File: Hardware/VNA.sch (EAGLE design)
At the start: 502 parts, among them IC1 MIC2253, IC10 MAX2871, IC11 RFSW6042, IC12 RFSW6042, IC13 QPC6324, IC14 RFSA3714, IC15 TRF37A73, IC16 QPC6324, IC17 QPC6324, IC18 QPC6324, IC19 AP2114H, IC2 LM3370SD-4221, IC20 NCP702-3.3, IC21 MAX2871, IC22 LT5560, IC23 THS4521IDGKR, IC24 ADL5801, IC25 NCP702-1.8, IC26 MCP33131D-10-E/MS, IC27 LT5560, IC28 THS4521IDGKR, IC29 ADL5801, IC3 LDL212PU50R, IC30 NCP702-1.8, IC31 MCP33131D-10-E/MS, IC32 THS4521IDGKR, IC33 ADL5801, IC34 NCP702-1.8, IC35 MCP33131D-10-E/MS, IC36 LT5560, IC37 STM32G431CB, IC4 LDL212PU50R, IC5 LDL212PU50R, IC6 LDL212PU50R, IC7 SI5351C, IC8 AP2114H, IC9 NCP702-3.3, J1 DNP, J2 AMPHENOL_132289, J3 AMPHENOL_132289, J4 TYPE-C16P(073), Q1 FA-128 26MHz, T1 B012-617DB-1-63-B331, T2 B012-617DB-1-63-B331, T3 B012-617DB-1-63-B331, U1 W25Q16BVSN, U2 6SLX9TQG144, X1 SMA_CONNECTOR, X2 SMA_CONNECTOR, X3 DNP

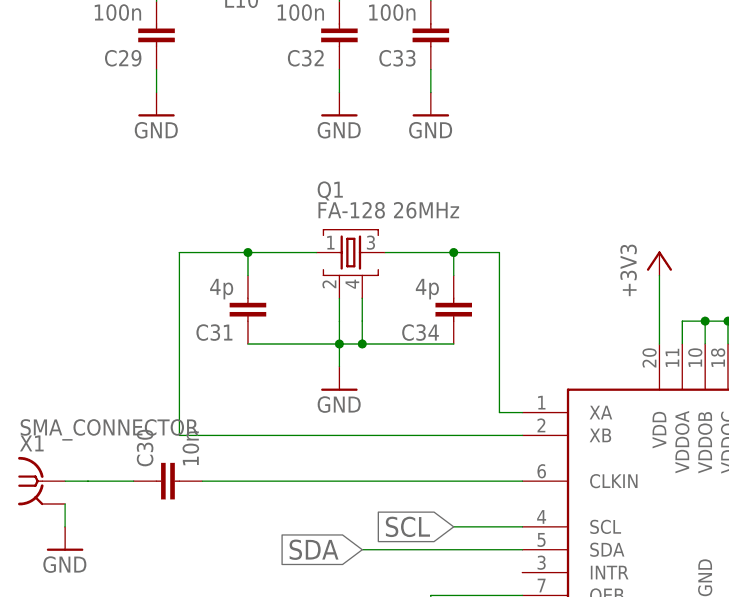
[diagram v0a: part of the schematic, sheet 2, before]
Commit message: TCXO instead of crystal
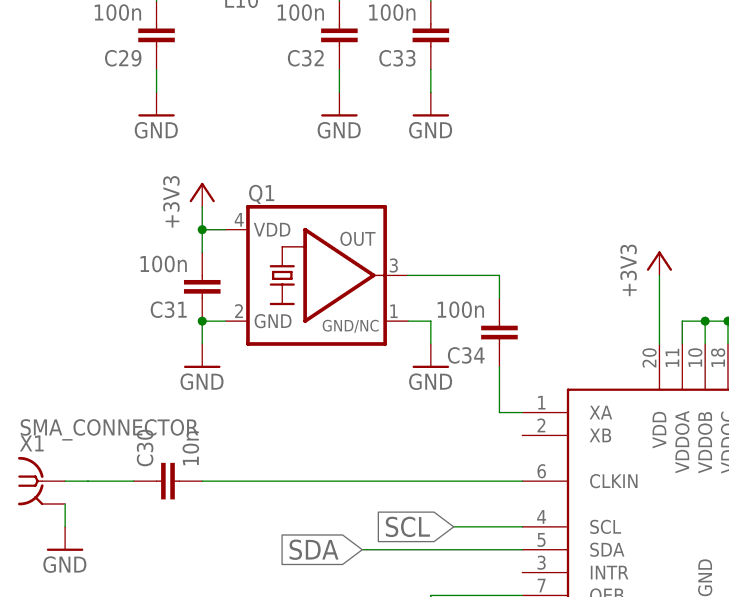
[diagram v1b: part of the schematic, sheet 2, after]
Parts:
- C31, C34: value 4p -> 100n
- Q1: value FA-128 26MHz -> DSB221SDN/26MHz; device VNA:FA-128 -> crystal-geyer_V1_0:KXO-TCXO-CMOS-86
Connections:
- net +3V3: now also C31.2, Q1.VDD
- net GND: now also Q1.GND, Q1.GND/NC; no longer C34.1, Q1.2, Q1.4
- net N$113: now also Q1.OUT; no longer IC7.XA, Q1.3
- net N$114: now also C34.1, IC7.XA; no longer C31.2, IC7.XB, Q1.1
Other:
- moved on the sheet: C31, C34
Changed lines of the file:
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@@
 <part name="R6" library="VNA" library_urn="urn:adsk.eagle:library:22367181" deviceset="R-EU_" device="R0402" package3d_urn="urn:adsk.eagle:package:22367274/2" value="10k"/>
 <part name="GND47" library="VNA" library_urn="urn:adsk.eagle:library:22367181" deviceset="GND" device=""/>
-<part name="Q1" library="VNA" library_urn="urn:adsk.eagle:library:22367181" deviceset="FA-" device="128" package3d_urn="urn:adsk.eagle:package:22367298/2" value="FA-128 26MHz"/>
-<part name="C31" library="VNA" library_urn="urn:adsk.eagle:library:22367181" deviceset="C-EU*?:2" device="C0402" package3d_urn="urn:adsk.eagle:package:22367275/2" value="4p"/>
-<part name="C34" library="VNA" library_urn="urn:adsk.eagle:library:22367181" deviceset="C-EU*?:2" device="C0402" package3d_urn="urn:adsk.eagle:package:22367275/2" value="4p"/>
+<part name="C31" library="VNA" library_urn="urn:adsk.eagle:library:22367181" deviceset="C-EU*?:2" device="C0402" package3d_urn="urn:adsk.eagle:package:22367275/2" value="100n"/>
+<part name="C34" library="VNA" library_urn="urn:adsk.eagle:library:22367181" deviceset="C-EU*?:2" device="C0402" package3d_urn="urn:adsk.eagle:package:22367275/2" value="100n"/>
 <part name="GND45" library="VNA" library_urn="urn:adsk.eagle:library:22367181" deviceset="GND" device=""/>
 <part name="L10" library="VNA" library_urn="urn:adsk.eagle:library:22367181" deviceset="INDUCTOR" device="0402" package3d_urn="urn:adsk.eagle:package:22367307/2" value="Ferrite"/>
@@
 <part name="C6" library="VNA" library_urn="urn:adsk.eagle:library:22367181" deviceset="C-EU*?:2" device="C0402" package3d_urn="urn:adsk.eagle:package:22367275/2" value="100n"/>
 <part name="GND13" library="VNA" library_urn="urn:adsk.eagle:library:22367181" deviceset="GND" device=""/>
+<part name="Q1" library="crystal-geyer_V1_0" library_urn="urn:adsk.eagle:library:203" deviceset="KXO-TCXO-CMOS" device="-86" package3d_urn="urn:adsk.eagle:package:11955/1" value="DSB221SDN/26MHz"/>
+<part name="GND262" library="VNA" library_urn="urn:adsk.eagle:library:22367181" deviceset="GND" device=""/>
+<part name="+3V1" library="VNA" library_urn="urn:adsk.eagle:library:22367181" deviceset="+3V3" device=""/>
 </parts>
 <sheets>
@@
 <attribute name="VALUE" x="91.44" y="106.68" size="1.778" layer="96"/>
 </instance>
-<instance part="Q1" gate="G$1" x="83.82" y="165.1" smashed="yes">
-<attribute name="NAME" x="81.28" y="171.196" size="1.778" layer="95"/>
-<attribute name="VALUE" x="81.28" y="168.91" size="1.778" layer="96"/>
-</instance>
-<instance part="C31" gate="G$1" x="73.66" y="157.48" smashed="yes" rot="R180">
-<attribute name="NAME" x="72.136" y="157.099" size="1.778" layer="95" rot="R180"/>
-<attribute name="VALUE" x="72.136" y="162.179" size="1.778" layer="96" rot="R180"/>
-</instance>
-<instance part="C34" gate="G$1" x="96.52" y="157.48" smashed="yes" rot="R180">
-<attribute name="NAME" x="94.996" y="157.099" size="1.778" layer="95" rot="R180"/>
-<attribute name="VALUE" x="94.996" y="162.179" size="1.778" layer="96" rot="R180"/>
-</instance>
-<instance part="GND45" gate="1" x="83.82" y="149.86" smashed="yes">
-<attribute name="VALUE" x="81.28" y="147.32" size="1.778" layer="96"/>
+<instance part="C31" gate="G$1" x="68.58" y="160.02" smashed="yes" rot="R180">
+<attribute name="NAME" x="67.056" y="159.639" size="1.778" layer="95" rot="R180"/>
+<attribute name="VALUE" x="67.056" y="164.719" size="1.778" layer="96" rot="R180"/>
+</instance>
+<instance part="C34" gate="G$1" x="101.6" y="154.94" smashed="yes" rot="R180">
+<attribute name="NAME" x="100.076" y="154.559" size="1.778" layer="95" rot="R180"/>
+<attribute name="VALUE" x="100.076" y="159.639" size="1.778" layer="96" rot="R180"/>
+</instance>
+<instance part="GND45" gate="1" x="68.58" y="152.4" smashed="yes">
+<attribute name="VALUE" x="66.04" y="149.86" size="1.778" layer="96"/>
 </instance>
 <instance part="L10" gate="G$1" x="71.12" y="195.58" smashed="yes" rot="R90">
@@
 <instance part="GND61" gate="1" x="259.08" y="88.9" smashed="yes">
 <attribute name="VALUE" x="256.54" y="86.36" size="1.778" layer="96"/>
+</instance>
+<instance part="Q1" gate="G$1" x="81.28" y="162.56" smashed="yes">
+<attribute name="NAME" x="73.66" y="170.815" size="1.778" layer="95"/>
+</instance>
+<instance part="GND262" gate="1" x="93.98" y="152.4" smashed="yes">
+<attribute name="VALUE" x="91.44" y="149.86" size="1.778" layer="96"/>
+</instance>
+<instance part="+3V1" gate="G$1" x="68.58" y="172.72" smashed="yes">
+<attribute name="VALUE" x="66.04" y="167.64" size="1.778" layer="96" rot="R90"/>
 </instance>
 </instances>
@@
 </segment>
 <segment>
-<pinref part="Q1" gate="G$1" pin="2"/>
-<wire x1="83.82" y1="160.02" x2="83.82" y2="157.48" width="0.1524" layer="91"/>
-<pinref part="GND45" gate="1" pin="GND"/>
-<wire x1="83.82" y1="152.4" x2="83.82" y2="154.94" width="0.1524" layer="91"/>
-<pinref part="C31" gate="G$1" pin="1"/>
-<wire x1="83.82" y1="154.94" x2="83.82" y2="157.48" width="0.1524" layer="91"/>
-<wire x1="73.66" y1="154.94" x2="83.82" y2="154.94" width="0.1524" layer="91"/>
-<junction x="83.82" y="154.94"/>
-<pinref part="C34" gate="G$1" pin="1"/>
-<wire x1="83.82" y1="154.94" x2="86.36" y2="154.94" width="0.1524" layer="91"/>
-<pinref part="Q1" gate="G$1" pin="4"/>
-<wire x1="86.36" y1="154.94" x2="96.52" y2="154.94" width="0.1524" layer="91"/>
-<wire x1="86.36" y1="157.48" x2="86.36" y2="160.02" width="0.1524" layer="91"/>
-<wire x1="86.36" y1="157.48" x2="86.36" y2="154.94" width="0.1524" layer="91"/>
-<junction x="86.36" y="154.94"/>
-</segment>
-<segment>
 <pinref part="GND43" gate="1" pin="GND"/>
 <pinref part="C29" gate="G$1" pin="1"/>
@@
 <pinref part="C47" gate="G$1" pin="2"/>
 <pinref part="GND61" gate="1" pin="GND"/>
+</segment>
+<segment>
+<pinref part="Q1" gate="G$1" pin="GND/NC"/>
+<pinref part="GND262" gate="1" pin="GND"/>
+<wire x1="91.44" y1="157.48" x2="93.98" y2="157.48" width="0.1524" layer="91"/>
+<wire x1="93.98" y1="157.48" x2="93.98" y2="154.94" width="0.1524" layer="91"/>
+</segment>
+<segment>
+<pinref part="GND45" gate="1" pin="GND"/>
+<pinref part="C31" gate="G$1" pin="1"/>
+<wire x1="68.58" y1="154.94" x2="68.58" y2="157.48" width="0.1524" layer="91"/>
+<pinref part="Q1" gate="G$1" pin="GND"/>
+<wire x1="71.12" y1="157.48" x2="68.58" y2="157.48" width="0.1524" layer="91"/>
+<junction x="68.58" y="157.48"/>
 </segment>
 </net>
@@
 <wire x1="93.98" y1="127" x2="104.14" y2="127" width="0.1524" layer="91"/>
 <pinref part="R6" gate="G$1" pin="2"/>
-</segment>
-</net>
-<net name="N$113" class="0">
-<segment>
-<pinref part="C34" gate="G$1" pin="2"/>
-<pinref part="Q1" gate="G$1" pin="3"/>
-<wire x1="96.52" y1="162.56" x2="96.52" y2="165.1" width="0.1524" layer="91"/>
-<wire x1="96.52" y1="165.1" x2="88.9" y2="165.1" width="0.1524" layer="91"/>
-<wire x1="96.52" y1="165.1" x2="101.6" y2="165.1" width="0.1524" layer="91"/>
-<wire x1="101.6" y1="165.1" x2="101.6" y2="147.32" width="0.1524" layer="91"/>
-<junction x="96.52" y="165.1"/>
-<pinref part="IC7" gate="G$1" pin="XA"/>
-<wire x1="101.6" y1="147.32" x2="104.14" y2="147.32" width="0.1524" layer="91"/>
-</segment>
-</net>
-<net name="N$114" class="0">
-<segment>
-<pinref part="Q1" gate="G$1" pin="1"/>
-<pinref part="C31" gate="G$1" pin="2"/>
-<wire x1="81.28" y1="165.1" x2="73.66" y2="165.1" width="0.1524" layer="91"/>
-<wire x1="73.66" y1="165.1" x2="73.66" y2="162.56" width="0.1524" layer="91"/>
-<pinref part="IC7" gate="G$1" pin="XB"/>
-<wire x1="104.14" y1="144.78" x2="66.04" y2="144.78" width="0.1524" layer="91"/>
-<wire x1="66.04" y1="144.78" x2="66.04" y2="165.1" width="0.1524" layer="91"/>
-<wire x1="66.04" y1="165.1" x2="73.66" y2="165.1" width="0.1524" layer="91"/>
-<junction x="73.66" y="165.1"/>
 </segment>
 </net>
@@
 <wire x1="119.38" y1="162.56" x2="119.38" y2="154.94" width="0.1524" layer="91"/>
 </segment>
+<segment>
+<pinref part="Q1" gate="G$1" pin="VDD"/>
+<wire x1="71.12" y1="167.64" x2="68.58" y2="167.64" width="0.1524" layer="91"/>
+<pinref part="C31" gate="G$1" pin="2"/>
+<wire x1="68.58" y1="167.64" x2="68.58" y2="165.1" width="0.1524" layer="91"/>
+<pinref part="+3V1" gate="G$1" pin="+3V3"/>
+<wire x1="68.58" y1="170.18" x2="68.58" y2="167.64" width="0.1524" layer="91"/>
+<junction x="68.58" y="167.64"/>
+</segment>
 </net>
 <net name="SCL" class="0">
@@
 </segment>
 </net>
+<net name="N$113" class="0">
+<segment>
+<pinref part="Q1" gate="G$1" pin="OUT"/>
+<pinref part="C34" gate="G$1" pin="2"/>
+<wire x1="91.44" y1="162.56" x2="101.6" y2="162.56" width="0.1524" layer="91"/>
+<wire x1="101.6" y1="162.56" x2="101.6" y2="160.02" width="0.1524" layer="91"/>
+</segment>
+</net>
+<net name="N$114" class="0">
+<segment>
+<pinref part="IC7" gate="G$1" pin="XA"/>
+<pinref part="C34" gate="G$1" pin="1"/>
+<wire x1="104.14" y1="147.32" x2="101.6" y2="147.32" width="0.1524" layer="91"/>
+<wire x1="101.6" y1="147.32" x2="101.6" y2="152.4" width="0.1524" layer="91"/>
+</segment>
+</net>

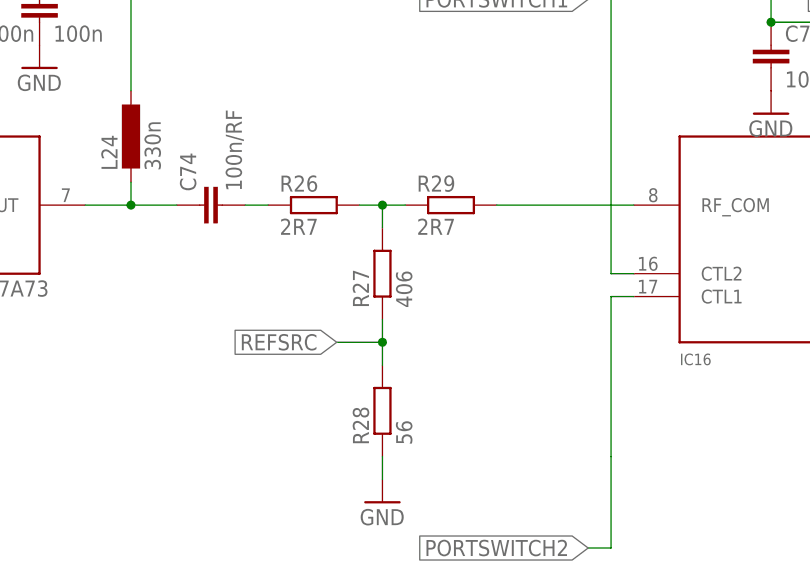
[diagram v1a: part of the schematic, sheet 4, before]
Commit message: R27 value fixed
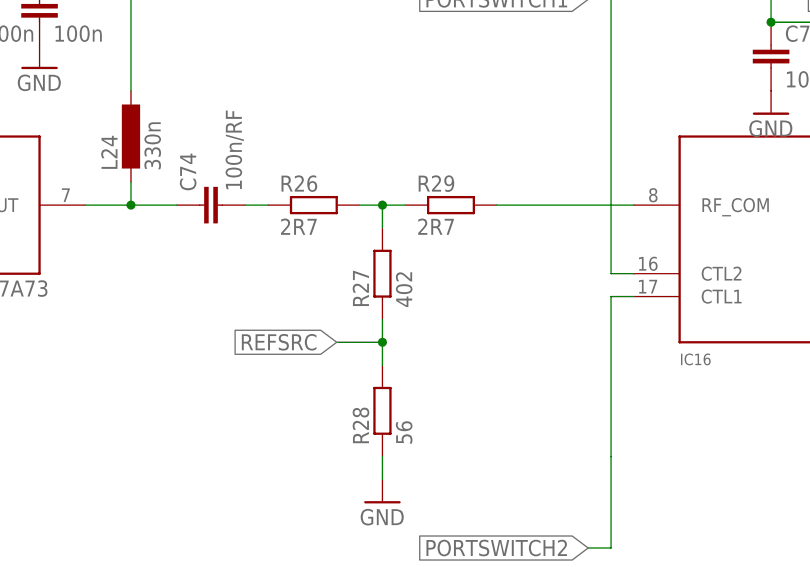
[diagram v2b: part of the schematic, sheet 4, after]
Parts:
- R27: value 406 -> 402
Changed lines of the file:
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@@
 <part name="R26" library="VNA" library_urn="urn:adsk.eagle:library:22367181" deviceset="R-EU_" device="R0402" package3d_urn="urn:adsk.eagle:package:22367274/2" value="2R7"/>
 <part name="R29" library="VNA" library_urn="urn:adsk.eagle:library:22367181" deviceset="R-EU_" device="R0402" package3d_urn="urn:adsk.eagle:package:22367274/2" value="2R7"/>
-<part name="R27" library="VNA" library_urn="urn:adsk.eagle:library:22367181" deviceset="R-EU_" device="R0402" package3d_urn="urn:adsk.eagle:package:22367274/2" value="406"/>
+<part name="R27" library="VNA" library_urn="urn:adsk.eagle:library:22367181" deviceset="R-EU_" device="R0402" package3d_urn="urn:adsk.eagle:package:22367274/2" value="402"/>
 <part name="R28" library="VNA" library_urn="urn:adsk.eagle:library:22367181" deviceset="R-EU_" device="R0402" package3d_urn="urn:adsk.eagle:package:22367274/2" value="56"/>
 <part name="GND103" library="VNA" library_urn="urn:adsk.eagle:library:22367181" deviceset="GND" device=""/>

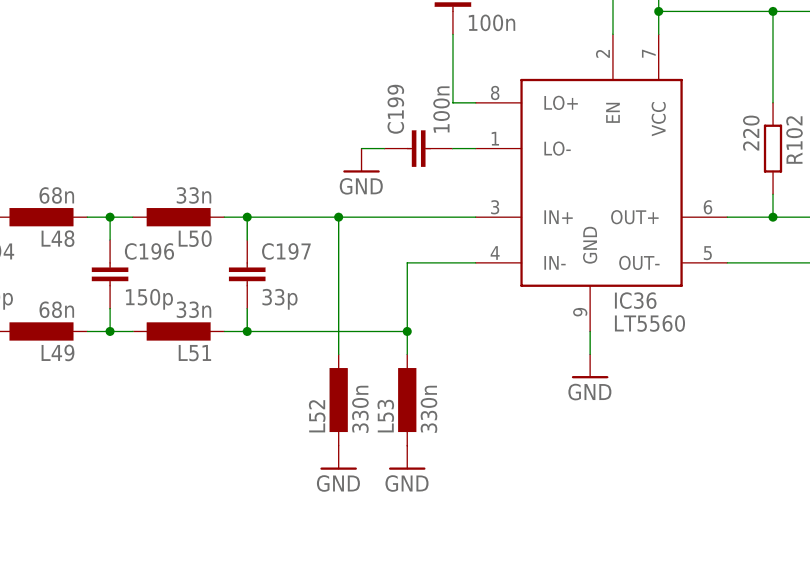
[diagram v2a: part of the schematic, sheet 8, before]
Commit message: Footprint adjustments for THS4521/0402 inductors, fixed mixup of CCLK/DIN
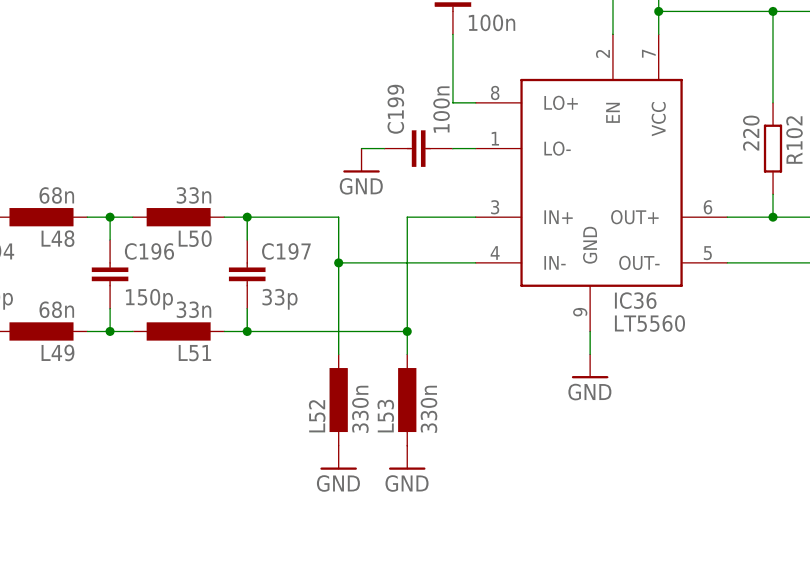
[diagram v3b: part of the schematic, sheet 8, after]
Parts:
- L10, L19, L20, L21, L22, L23, L25, L26, L27, L28, L29: device VNA:INDUCTOR0402 -> VNA:FERRITE
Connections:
- net MCU_FPGA_CCLK: now also IC37.PB13; no longer IC37.PB15
- net MCU_FPGA_DIN: now also IC37.PB15; no longer IC37.PB13
- net N$86: now also IC36.IN-; no longer IC36.IN+
- net N$87: now also IC36.IN+; no longer IC36.IN-

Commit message: DC jack with power priority over USB
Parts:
- removed X3: DNP, VNA:MINI-USB-SCHIELD-32005-301
- added Q2: SSM3J338R, VNA:SSM3J338R
- added Y1: DSB221SDN/26MHz, crystal-geyer_V1_0:KXO-TCXO-CMOS-86
- J1: value DNP -> PJ-014D; device VNA:DCJ0202 -> VNA:PJ-014D
- Q1: value DSB221SDN/26MHz -> SSM3J338R; device crystal-geyer_V1_0:KXO-TCXO-CMOS-86 -> VNA:SSM3J338R
- R125: value 0 -> 10k
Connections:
- removed net N$185: J4.VBUS, R125.1
- new net N$167: Q1.S, Q2.S, R125.2
- new net N$168: J1.2, Q1.G, Q2.G, R125.1
- new net USB_POWER: J4.VBUS, Q1.D
- net +3V3: now also Y1.VDD; no longer Q1.VDD
- net +5V: now also Q2.D; no longer R125.2
- net GND: now also Y1.GND, Y1.GND/NC; no longer Q1.GND, Q1.GND/NC, X3G$1.5, X3S.S1, X3S.S2, X3S.S3, X3S.S4
- net N$113: now also Y1.OUT; no longer Q1.OUT
- net N$186: no longer X3G$1.3
- net N$189: no longer X3G$1.2
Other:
- moved on the sheet: C1, C10, C11, C12, C13, C14, C15, C16, C17, C18, C19, C2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

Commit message: Updated BOM
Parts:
- C18: device VNA:C-EUC0603 -> VNA:C-EUC0603:1
- L6, L7, L8, L9: device VNA:INDUCTOR0402 -> VNA:FERRITE

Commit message: Schematic PDF
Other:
- note added: "1.LO"
- note added: "Attenuator/Amplifier/Switches"
- note added: "FPGA Connections"
- note added: "HF Source"
- note added: "Power Supply"
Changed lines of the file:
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@@
 <text x="345.44" y="71.12" size="1.778" layer="97">Source and 1.LO, up to 350mA</text>
 <text x="198.12" y="88.9" size="1.778" layer="97">I2C address: 0x42</text>
+<text x="342.9" y="20.32" size="2.54" layer="94">Power Supply</text>
 </plain>
 <instances>
@@
 <text x="337.82" y="121.92" size="1.778" layer="97">ca. 2dbm</text>
 <text x="297.18" y="177.8" size="1.778" layer="97">C1/C2 should not be driven above 1.8V</text>
+<text x="342.9" y="20.32" size="2.54" layer="94">HF Source</text>
 </plain>
 <instances>
@@
 <text x="142.24" y="129.54" size="1.778" layer="97">ca. -30 to 0dbm</text>
 <text x="172.72" y="185.42" size="1.778" layer="97">Up to 60mA on 3V3</text>
+<text x="342.9" y="20.32" size="2.1844" layer="94">Attenuator/Amplifier/Switches</text>
 </plain>
 <instances>
@@
 <text x="119.38" y="215.9" size="1.778" layer="97">3x 3V3</text>
 <text x="226.06" y="73.66" size="1.778" layer="97">Approx. 450kHz loop bandwidth</text>
+<text x="342.9" y="20.32" size="2.54" layer="94">1.LO</text>
 </plain>
 <instances>
@@
 <sheet>
 <plain>
+<text x="342.9" y="20.32" size="2.54" layer="94">FPGA Connections</text>
 </plain>
 <instances>
